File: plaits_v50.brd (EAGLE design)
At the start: 59 x 106.7 mm, 162 parts, among them IC1 R-78E3.3-0.5, IC2 TLC59281DBQ, IC3 LD2981ABU33, IC4 STM32F373CCT6, IC5 PCM5100APW, IC6 MCP6004, IC7 MCP6004, IC8 TL072PW, IC9 LM4040B10, J1 PJ301_THONKICONN6, J10 PJ301_THONKICONN6, J2 PJ301_THONKICONN6, J3 PJ301_THONKICONN6, J4 PJ301_THONKICONN6, J5 PJ301_THONKICONN6, J6 PJ301_THONKICONN6, J7 PJ301_THONKICONN6, J8 PJ301_THONKICONN6, J9 PJ301_THONKICONN6, Q1 8MHz

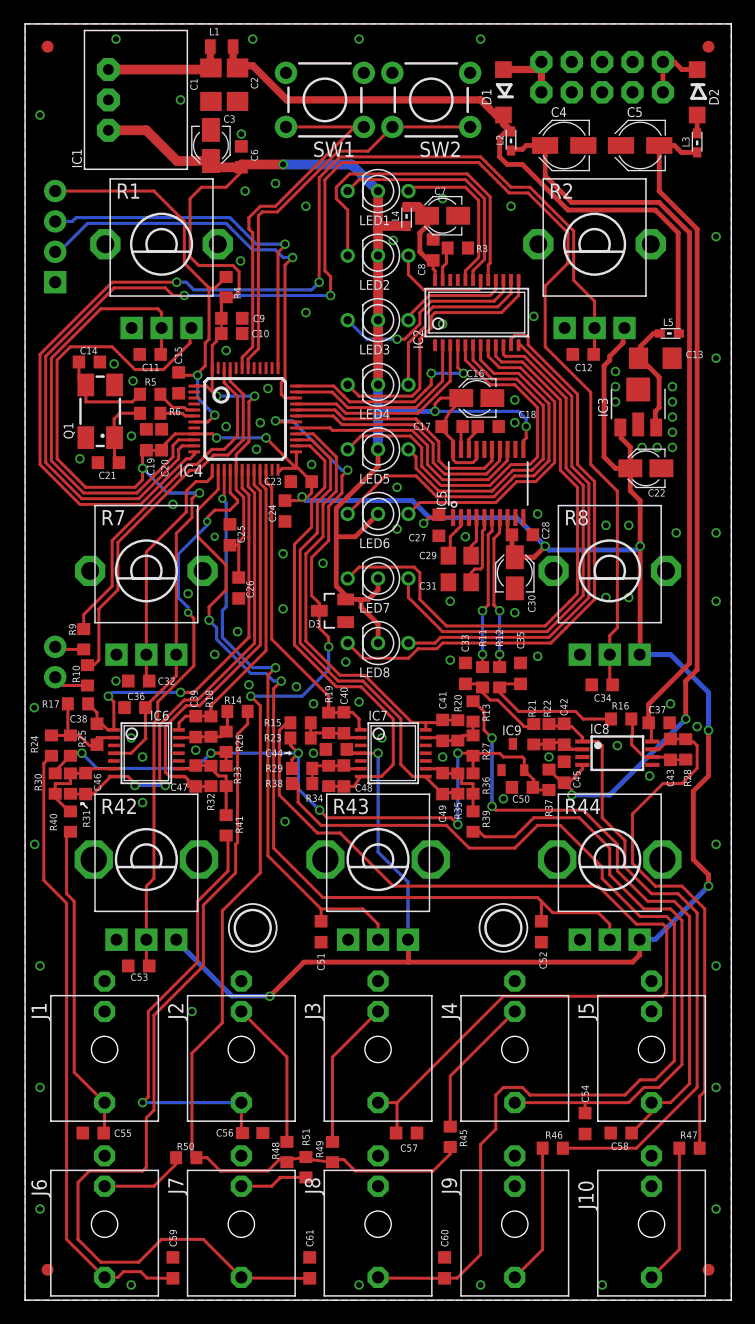
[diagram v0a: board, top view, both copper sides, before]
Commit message: Fixed potential clearance issues
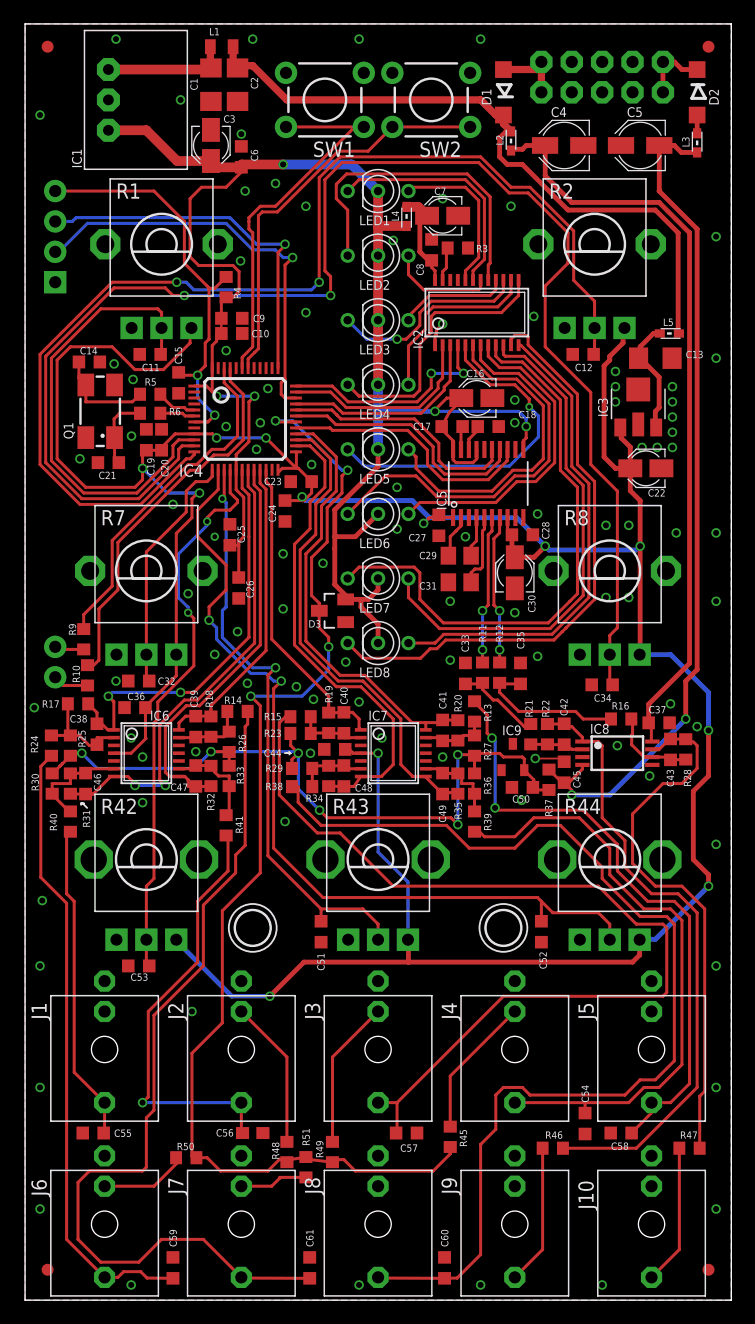
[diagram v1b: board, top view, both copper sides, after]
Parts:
- moved R15 0.51 mm to (23.1, 48.8)
- moved R11 0.38 mm to (38.3, 52.5)
- moved R12 0.38 mm to (39.7, 52.5)
- moved R23 0.38 mm to (23.1, 47.4)
- moved R21 0.25 mm to (42.3, 47.3)
- moved R30 0.25 mm to (2.29, 43.2)
- moved R26 0.25 mm to (17.1, 46.7)
- moved R33 0.25 mm to (17.1, 43.8)
- moved R38 0.25 mm to (23.2, 42.9)
- moved C8 0.13 mm to (34.0, 87.8)
- moved R36 0.13 mm to (37.6, 43.2)
- moved C44 0.13 mm to (25.9, 46.0)
- moved R13 0.13 mm to (37.6, 49.2)
- moved R22 0.13 mm to (43.7, 47.3)
- moved R27 0.13 mm to (37.6, 46.4)
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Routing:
- net GND: track 2.19 -> 6.75 mm
- net N$22: track 33.0 -> 28.9 mm, vias 0 -> 1
- net FM_IN: track 79.5 -> 80.1 mm
- net AREF_-10: track 64.5 -> 65.1 mm
